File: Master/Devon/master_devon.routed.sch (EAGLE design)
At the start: 36 parts, among them J1 ISP, K1 653002114822, K2 653002114822, K3 653002114822, K4 653002114822, U1 ATMEGA128RFA1, U2 ULN2003ADR, Y1 16MHz

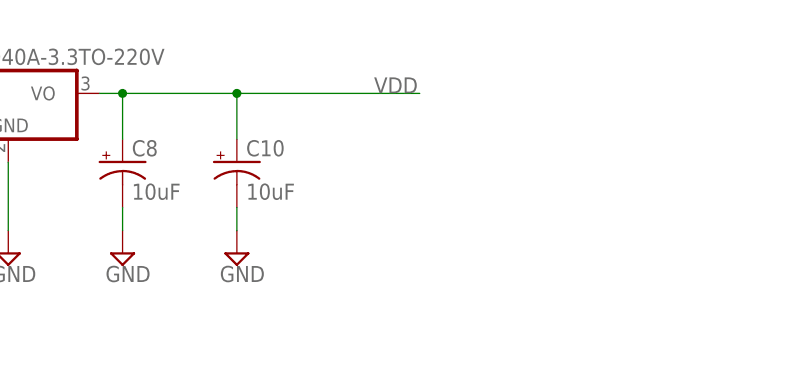
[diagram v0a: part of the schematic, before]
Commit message: Made board smaller, fixed VDD->3.3V issue
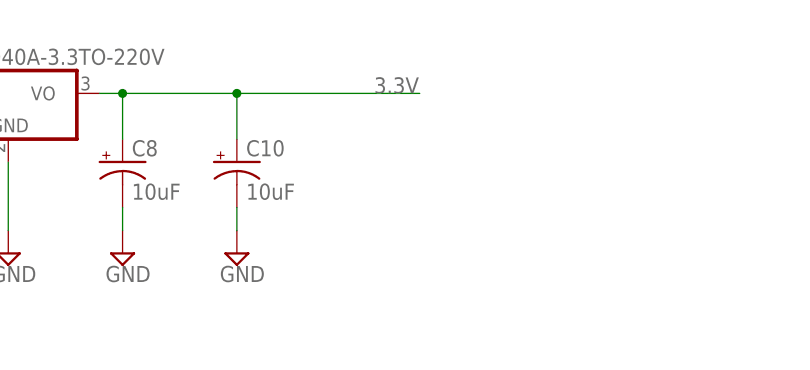
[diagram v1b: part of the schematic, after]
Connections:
- removed net VDD: C10.+, C8.+, U$2.VO
- net 3.3V: now also C10.+, C8.+, U$2.VO
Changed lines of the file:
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@@
 <label x="91.44" y="162.56" size="1.778" layer="95"/>
+</segment>
+<segment>
+<pinref part="U$2" gate="G$1" pin="VO"/>
+<wire x1="93.98" y1="241.3" x2="96.52" y2="241.3" width="0.1524" layer="91"/>
+<pinref part="C8" gate="G$1" pin="+"/>
+<wire x1="96.52" y1="241.3" x2="109.22" y2="241.3" width="0.1524" layer="91"/>
+<wire x1="109.22" y1="241.3" x2="129.54" y2="241.3" width="0.1524" layer="91"/>
+<wire x1="96.52" y1="236.22" x2="96.52" y2="241.3" width="0.1524" layer="91"/>
+<junction x="96.52" y="241.3"/>
+<label x="124.46" y="241.3" size="1.778" layer="95"/>
+<pinref part="C10" gate="G$1" pin="+"/>
+<wire x1="109.22" y1="236.22" x2="109.22" y2="241.3" width="0.1524" layer="91"/>
+<junction x="109.22" y="241.3"/>
 </segment>
 </net>
@@
 </segment>
 </net>
-<net name="VDD" class="0">
-<segment>
-<pinref part="U$2" gate="G$1" pin="VO"/>
-<wire x1="93.98" y1="241.3" x2="96.52" y2="241.3" width="0.1524" layer="91"/>
-<pinref part="C8" gate="G$1" pin="+"/>
-<wire x1="96.52" y1="241.3" x2="109.22" y2="241.3" width="0.1524" layer="91"/>
-<wire x1="109.22" y1="241.3" x2="129.54" y2="241.3" width="0.1524" layer="91"/>
-<wire x1="96.52" y1="236.22" x2="96.52" y2="241.3" width="0.1524" layer="91"/>
-<junction x="96.52" y="241.3"/>
-<label x="124.46" y="241.3" size="1.778" layer="95"/>
-<pinref part="C10" gate="G$1" pin="+"/>
-<wire x1="109.22" y1="236.22" x2="109.22" y2="241.3" width="0.1524" layer="91"/>
-<junction x="109.22" y="241.3"/>
-</segment>
-</net>
